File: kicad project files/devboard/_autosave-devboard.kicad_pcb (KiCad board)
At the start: 2 copper layers, 21 x 51 mm, 33 parts, among them J1 USB_C_Receptacle_USB2.0_14P, J2 Conn_01x20, J3 Conn_01x20, J4 Conn_01x03, SW1 SW_Push, U1 RP2040, U2 MCP1700x-330xxTT, U3 W25Q128JVS, Y1 12 MHz

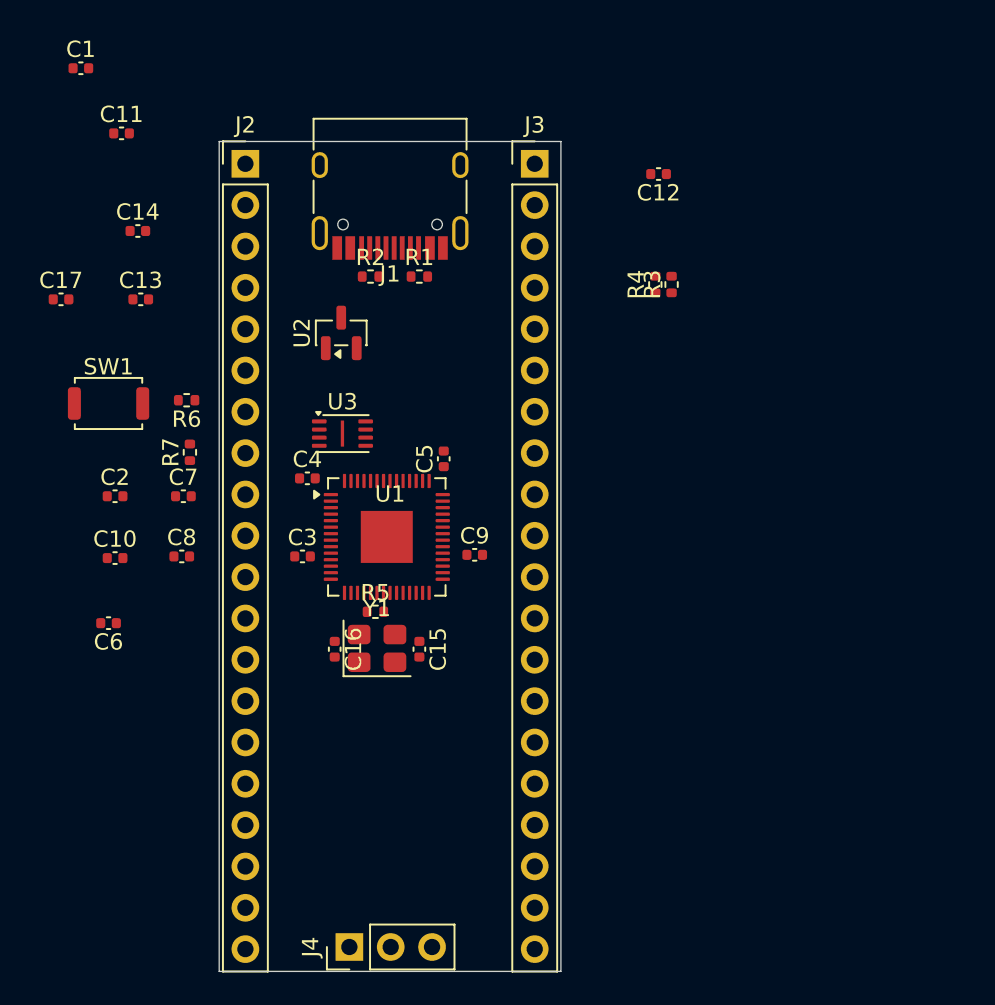
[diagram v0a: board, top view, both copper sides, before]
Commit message: finished schematic, worked on pcb design
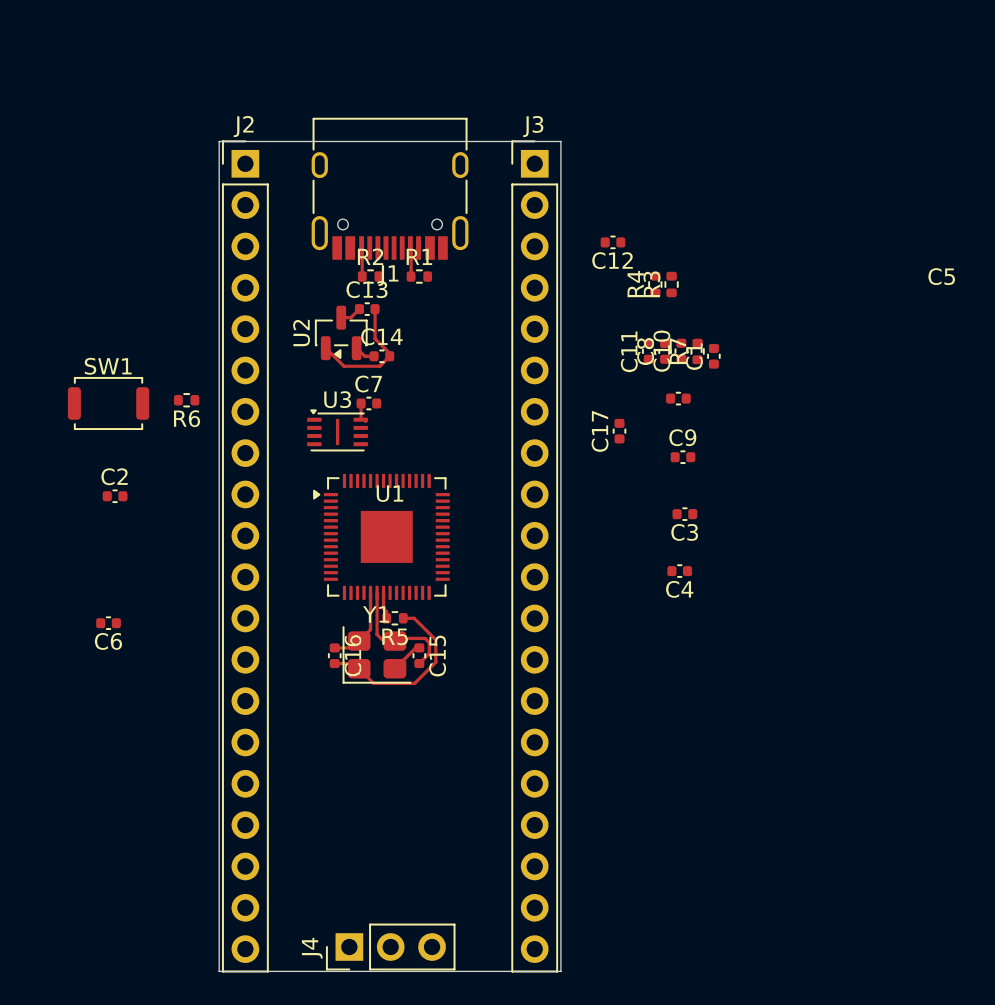
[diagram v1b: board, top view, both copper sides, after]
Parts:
- moved C1 42.7 mm to (230.4, 73.2), turned to 90 degrees
- moved C10 37.1 mm to (228.4, 72.9), turned to 90 degrees
- moved C17 35.3 mm to (224.6, 77.8), turned to 90 degrees
- moved C11 35.1 mm to (226.4, 72.9), turned to 90 degrees
- moved C8 32.3 mm to (227.4, 72.9), turned to 90 degrees
- moved R7 31.8 mm to (229.4, 72.9)
- moved C3 23.6 mm to (228.6, 82.9), turned to 180 degrees
- moved C4 23.6 mm to (228.3, 86.4), turned to 180 degrees
- moved C14 16.9 mm to (210.0, 73.2)
- moved C5 14.9 mm to (228.2, 75.8), turned to 0 degrees
- moved C9 14.1 mm to (228.5, 79.4)
- moved C13 13.9 mm to (209.1, 70.3)
- moved C7 12.7 mm to (209.2, 76.1)
- moved C12 5.05 mm to (224.2, 66.2)
- moved R5 1.26 mm to (210.8, 89.3), turned to 180 degrees
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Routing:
- net GND: track 0.00 -> 14.9 mm
- net Net-(C16-Pad2): track 0.00 -> 11.2 mm
- net XIN: track 0.00 -> 7.65 mm
- net +3V3: track 0.00 -> 2.31 mm
- net Net-(J1-CC2): track 0.00 -> 1.77 mm
- net Net-(J1-CC1): track 0.00 -> 1.77 mm
- net XOUT: track 0.00 -> 1.64 mm
- net VBUS: track 0.00 -> 1.34 mm
